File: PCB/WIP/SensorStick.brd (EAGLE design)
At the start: 74.9 x 39.4 mm, 84 parts, among them U1 TPD4F003DQDR, U10 LIS3MDLTR, U11 LIS3MDLTR, U2 BMI088, U3 BMI088, U4 BMI088, U5 STM32H743ZIT6, U9 LIS3MDLTR, Y1 ECS-TXO-3225MV-400-TR

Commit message: starting on board
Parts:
- removed AIRSPEED: 4525DO-DS5AI001DP, 4525DO-DS5AI001DP:4525DO-DS...P
- removed C3: 0.1uF, SparkFun-Capacitors:0402
- added R19, R20, R21, R22: RT0402FRE07220RL, ce-capstone:RESC1005X35N
- R6, R7: value 4.7k -> RT0402FRE07220RL; device SparkFun-Resistors:0603 -> ce-capstone:RESC1005X35N
- moved U10 561.4 mm to (62.0, 37.3)
- moved C36 544.9 mm to (14.7, 36.3)
- moved C35 536.1 mm to (9.14, 36.3)
- moved C34 502.8 mm to (11.7, 10.4)
- moved R10 501.0 mm to (53.8, 17.8)
- moved FL3 500.4 mm to (54.1, 20.1)
- moved U3 493.0 mm to (21.6, 30.7)
- moved C31 492.7 mm to (59.2, 24.4)
- moved U9 490.1 mm to (48.8, 8.13)
- moved C30 489.7 mm to (59.2, 29.5)
- moved FL1 486.2 mm to (70.9, 17.8)
- moved C29 480.3 mm to (59.2, 18.5)
- moved U11 474.0 mm to (8.13, -6.35)
- moved C32 470.2 mm to (51.1, -6.60)
- moved C33 467.9 mm to (43.7, -6.10)
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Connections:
- new net N$13: R6.2, U5.123
- new net N$14: R7.2, U5.122
- net 3V3: no longer R6.2, R7.1
- net 5V: no longer AIRSPEED.2, C3.2
- net CSB_ACCEL1: now also R19.2
- net CSB_ACCEL2: now also R21.2
- net CSB_ACCEL3: now also R6.1
- net CSB_GYRO1: now also R20.2
- net CSB_GYRO2: now also R7.1
- net CSB_GYRO3: now also U5.79
- net EXTI3: no longer AIRSPEED.5
- net GND: now also Y1.2; no longer AIRSPEED.1, C3.1
- net I2C3_SCL: no longer AIRSPEED.4, R6.1
- net I2C3_SDA: no longer AIRSPEED.3, R7.2
- net SPI1_MISO: no longer U4.10
- net SPI2_MISO: no longer U3.10
- net SPI3_MISO: no longer U2.10
- net USART2_RX: now also U5.37
- net USART2_TX: now also U5.36
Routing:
- net GND: track 69.6 -> 253.4 mm, vias 20 -> 29
- net 3V3: track 47.4 -> 206.3 mm, vias 11 -> 21
- net I2C1_SCL: track 0.00 -> 135.8 mm, vias 0 -> 7
- net I2C1_SDA: track 0.00 -> 120.3 mm, vias 0 -> 7
- net EXTI0: track 0.00 -> 101.9 mm, vias 0 -> 7
- net SPI2_MISO: track 0.00 -> 97.8 mm, vias 0 -> 6
- net EXTI2: track 0.00 -> 93.2 mm, vias 0 -> 6
- net 3V5: track 0.00 -> 87.1 mm, vias 0 -> 3
- net SPI2_SCK: track 0.00 -> 82.4 mm, vias 0 -> 2
- net SPI2_MOSI: track 0.00 -> 81.7 mm, vias 0 -> 6
- net CSB_ACCEL2: track 0.00 -> 80.7 mm, vias 0 -> 4
- net I2C3_SDA: track 23.0 -> 97.6 mm, vias 2 -> 4
- net I2C2_SCL: track 0.00 -> 73.3 mm, vias 0 -> 6
- net 3V2: track 0.00 -> 70.7 mm, vias 0 -> 4
- net IMU_INT4: track 0.00 -> 69.3 mm, vias 0 -> 8
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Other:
- board size 74.9 x 39.4 mm -> 79.5 x 48.3 mm
- board text removed: "AIR"
- board text removed: "IMU"
- board text removed: "Jesus Oviedo Noah Lutz Teagan Connon Marko Ristic Danny Cardenas"
- board text removed: "Project Dragonfly UCSB CE Capstone"

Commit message: snapshot
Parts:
- removed R22: RT0402FRE07220RL, ce-capstone:RESC1005X35N
- moved R21 112.5 mm to (72.4, 45.7)
- moved R20 110.7 mm to (54.6, 59.7), turned to 90 degrees
- moved R7 103.9 mm to (74.9, 45.7)
- moved R19 97.9 mm to (47.0, 52.1)
- moved R11 96.5 mm to (33.0, 69.8)
- moved Y1 86.0 mm to (26.7, 68.6)
- moved R9 80.1 mm to (22.9, 47.0)
- moved R8 73.4 mm to (22.9, 43.2)
- moved S2 72.0 mm to (68.6, 67.3)
- moved R3 71.4 mm to (74.9, 20.3), turned to 90 degrees
- moved D1 70.7 mm to (74.9, 25.4), turned to 90 degrees
- moved U$1 70.0 mm to (57.1, 69.8), turned to 0 degrees
- moved JST_CONNECTION 67.3 mm to (39.4, 68.6), turned to 0 degrees
- moved R6 66.1 mm to (68.6, 62.2)
- moved U11 63.7 mm to (26.7, 54.6)
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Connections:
- net SPI1_CS renamed JTDI
- new net JTRST: U5.134
- new net TRACESWO: U5.133
- net NRST: now also U5.25
- net SPI3_MISO: now also U5.112; no longer U5.134
- net SPI3_SCK: now also U5.111; no longer U5.133
- net SWCLK: now also U5.109
- net SWDIO: now also U5.105
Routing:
- net GND: track 253.4 -> 0.00 mm, vias 29 -> 0
- net 3V3: track 206.3 -> 0.00 mm, vias 21 -> 0
- net I2C1_SCL: track 135.8 -> 0.00 mm, vias 7 -> 0
- net I2C1_SDA: track 120.3 -> 0.00 mm, vias 7 -> 0
- net EXTI0: track 101.9 -> 0.00 mm, vias 7 -> 0
- net SPI2_MISO: track 97.8 -> 0.00 mm, vias 6 -> 0
- net I2C3_SDA: track 97.6 -> 0.00 mm, vias 4 -> 0
- net EXTI2: track 93.2 -> 0.00 mm, vias 6 -> 0
- net 3V5: track 87.1 -> 0.00 mm, vias 3 -> 0
- net GPIO_EXTI1: track 86.8 -> 0.00 mm, vias 3 -> 0
- net I2C3_SCL: track 83.5 -> 0.00 mm, vias 4 -> 0
- net SPI2_SCK: track 82.4 -> 0.00 mm, vias 2 -> 0
- net SPI2_MOSI: track 81.7 -> 0.00 mm, vias 6 -> 0
- net 5V: track 81.2 -> 0.00 mm
- net CSB_ACCEL2: track 80.7 -> 0.00 mm, vias 4 -> 0
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- removed copper zone on layer 15, net 3V3
- removed copper zone on layer 2, net GND
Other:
- board size 79.5 x 48.3 mm -> 77.5 x 74.6 mm
- board text removed: "**. ., ,,. ,. , *. .,. .. ,, ,. , ., ............ , ,, ., *., ** ,, .. , . ., ,, .. ., ,. ,,, *, , ./ ., ., , * .,. * ,, ,, *. .......... ...,. (*,. , ./, */. .*/ * ** .,*//,. .*/*, .* ,,. . . .* . */*/*. , ,. . , . ,. *,,*. .,,. .,, ,. .. , . ,*/,. .* .. ...,,,.. ..,. * .,. , . ,.,*. . .,./ , ..,, ,. ,,. ..,* ,*.. .,. .. ,., . , ...,,,,.. ...,,,.,,,,.... ....,.... ,, .. , * ,.,, .. ,, .. . * , *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"
- board text removed: "1"
- board text removed: "BAR"
- board text removed: "BOOT0"
- board text removed: "GPS"
- board text removed: "JST"
- board text removed: "MAG"
- board text removed: "NRST"
- board text removed: "PWR"
- board text removed: "RST"
- board text removed: "SWCLK"
- board text removed: "SWDIO"
- board text removed: "SWO"
- board text removed: "TX"

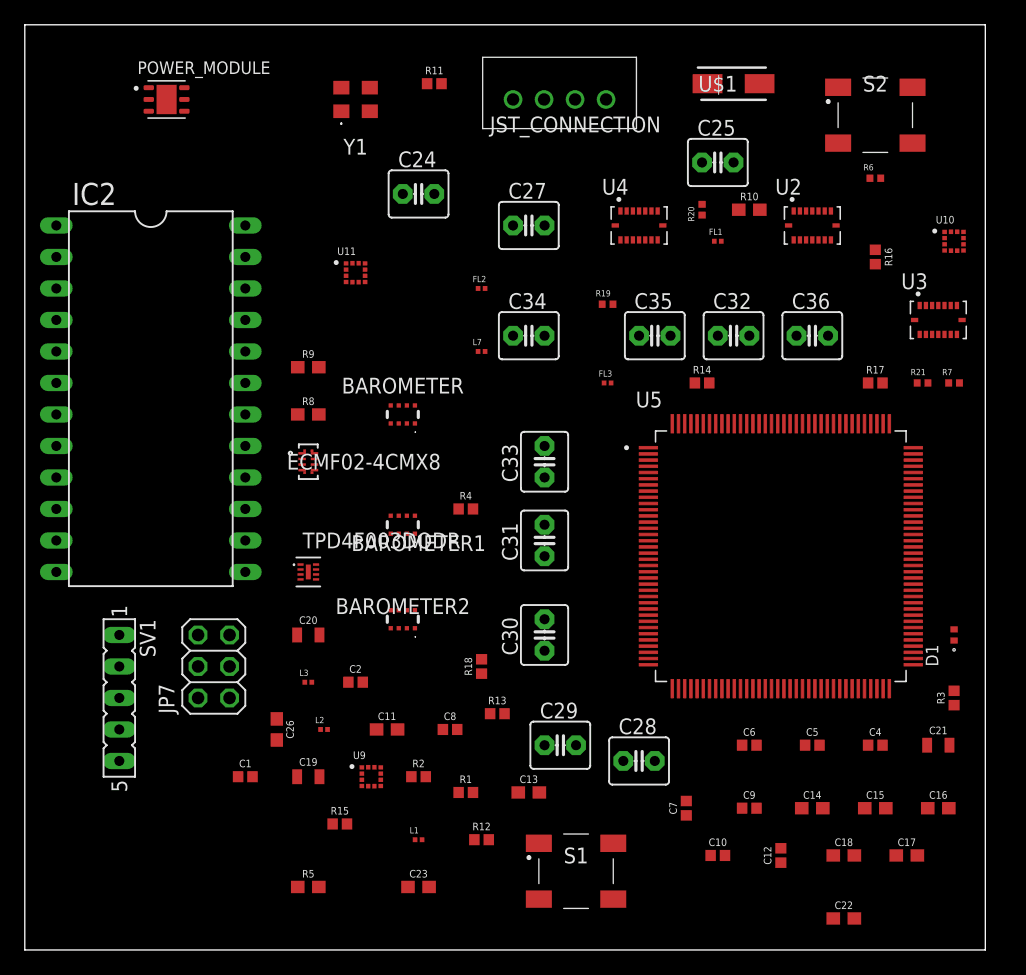
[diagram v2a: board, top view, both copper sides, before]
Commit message: added in JST connections, still need to resolve extra SPI connection
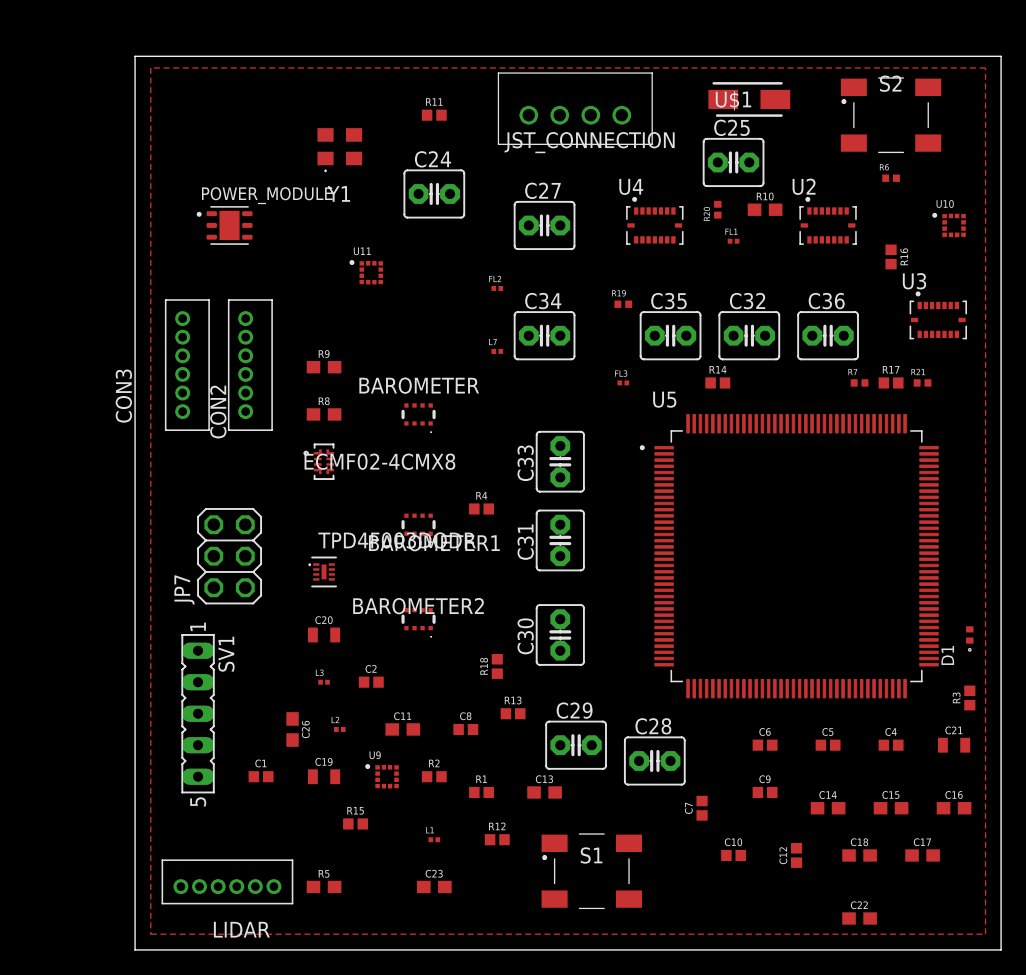
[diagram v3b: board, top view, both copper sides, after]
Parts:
- removed IC2: (no value), ic-package:DIL24-6
- added CON2, CON3, LIDAR: B6B-ZR, jst:B6B-ZR
- moved POWER_MODULE 11.4 mm to (16.5, 58.4)
- moved JP7 8.98 mm to (16.5, 31.8)
- moved R7 7.62 mm to (67.3, 45.7)
- moved SV1 6.48 mm to (14.0, 19.1)
- moved Y1 4.02 mm to (25.4, 64.8)
- moved R11 2.54 mm to (33.0, 67.3)
- moved JST_CONNECTION 1.80 mm to (40.6, 67.3)
- moved U$1 1.80 mm to (58.4, 68.6)
- moved C9 1.80 mm to (59.7, 12.7)
- moved C16 1.27 mm to (74.9, 11.4)
- moved C21 1.27 mm to (74.9, 16.5)
- moved C23 1.27 mm to (33.0, 5.08)
- moved C24 1.27 mm to (33.0, 61.0)
- moved C29 1.27 mm to (44.5, 16.5)
- moved C30 1.27 mm to (43.2, 25.4)
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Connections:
- new net N$21: LIDAR.5
- new net N$22: LIDAR.4
- net 3V3: now also LIDAR.1; no longer IC2.1, IC2.2
- net EXTI4: no longer IC2.15
- net GND: now also LIDAR.6; no longer IC2.13
- net I2C1_SCL: no longer IC2.20
- net I2C1_SDA: no longer IC2.21
- net I2C4_SCL: now also LIDAR.2
- net I2C4_SDA: now also LIDAR.3, U5.82
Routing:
- added copper zone on layer 1, net 3V3
- added copper zone on layer 2, net GND
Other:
- board size 77.5 x 74.6 mm -> 69.8 x 72.1 mm

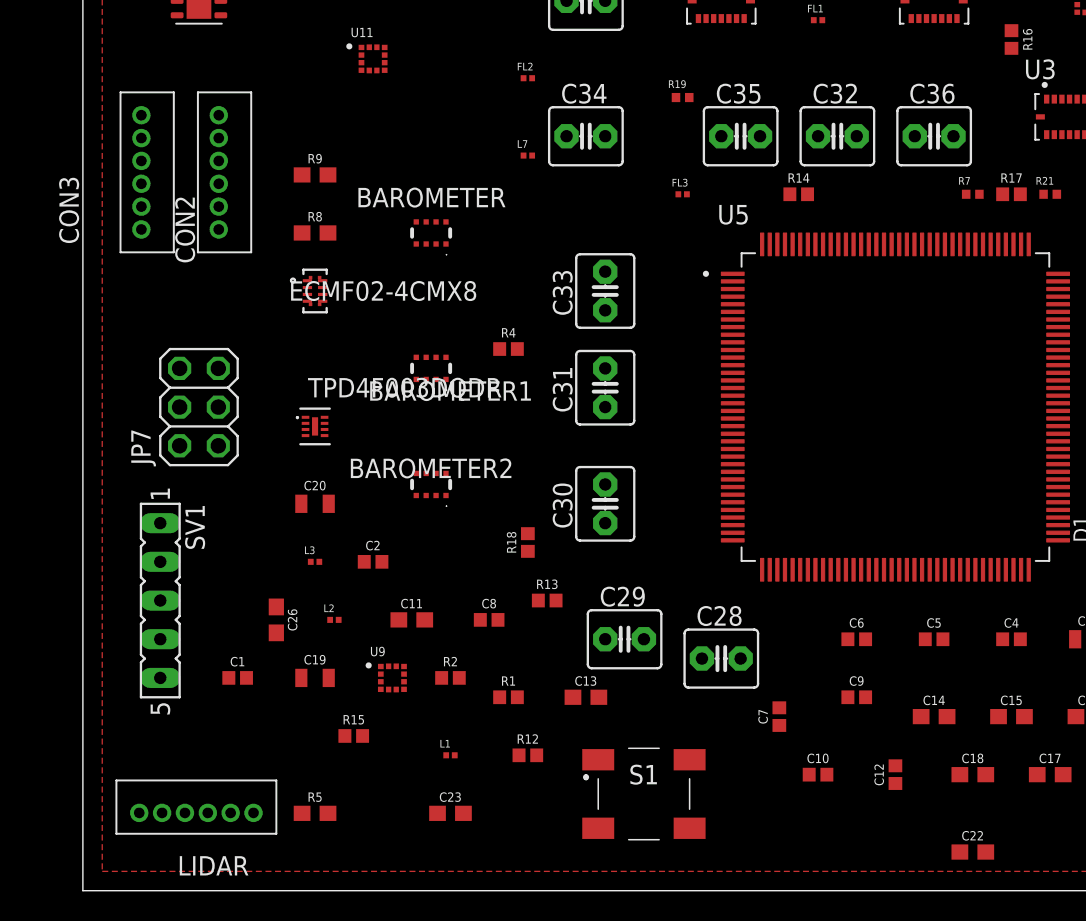
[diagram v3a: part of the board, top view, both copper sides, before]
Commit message: all jsts added, board mostly laid out, working on connections now
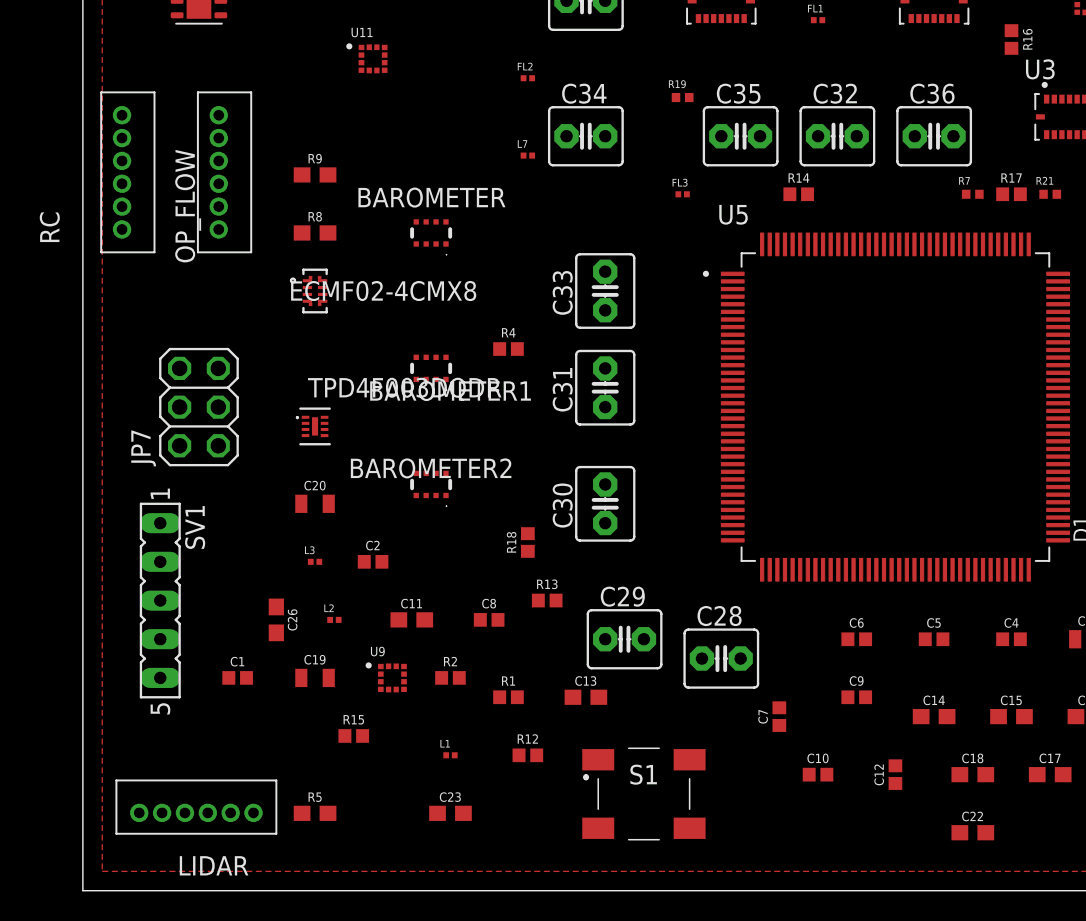
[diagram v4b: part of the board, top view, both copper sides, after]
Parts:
- removed CON3: B6B-ZR, jst:B6B-ZR
- added RC: B6B-ZR, jst:B6B-ZR
- moved C22 1.27 mm to (67.3, 3.81)
- renumbered CON2 to OP_FLOW
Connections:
- new net N$18: RC.4
- new net N$19: RC.5
- net 3V3: now also OP_FLOW.1, RC.1
- net GND: now also OP_FLOW.6, RC.6
- net SPI6_CS: now also OP_FLOW.5
- net SPI6_MISO: now also OP_FLOW.3
- net SPI6_MOSI: now also OP_FLOW.4
- net SPI6_SCK: now also OP_FLOW.2
- net UART5_RX: now also RC.3
- net UART5_TX: now also RC.2

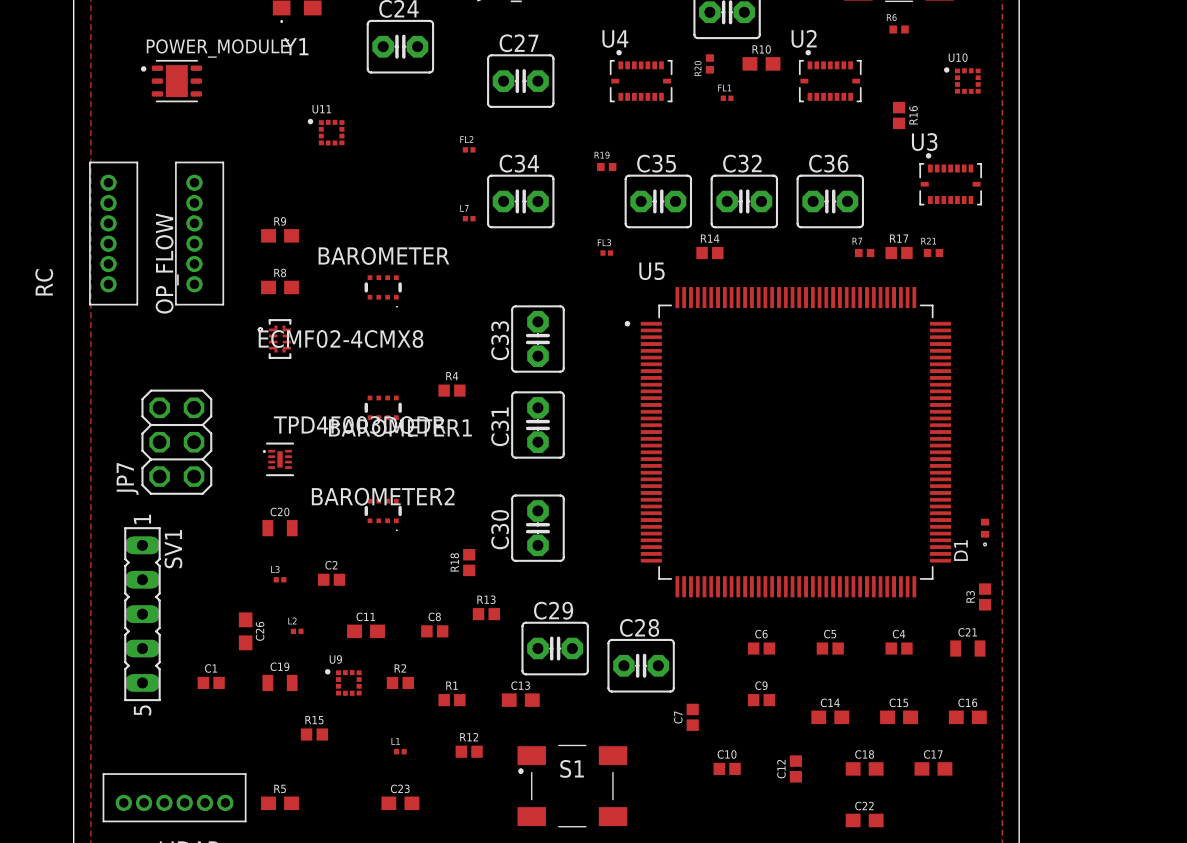
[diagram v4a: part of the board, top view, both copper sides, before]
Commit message: some minor changes with VDD, VBAT connections
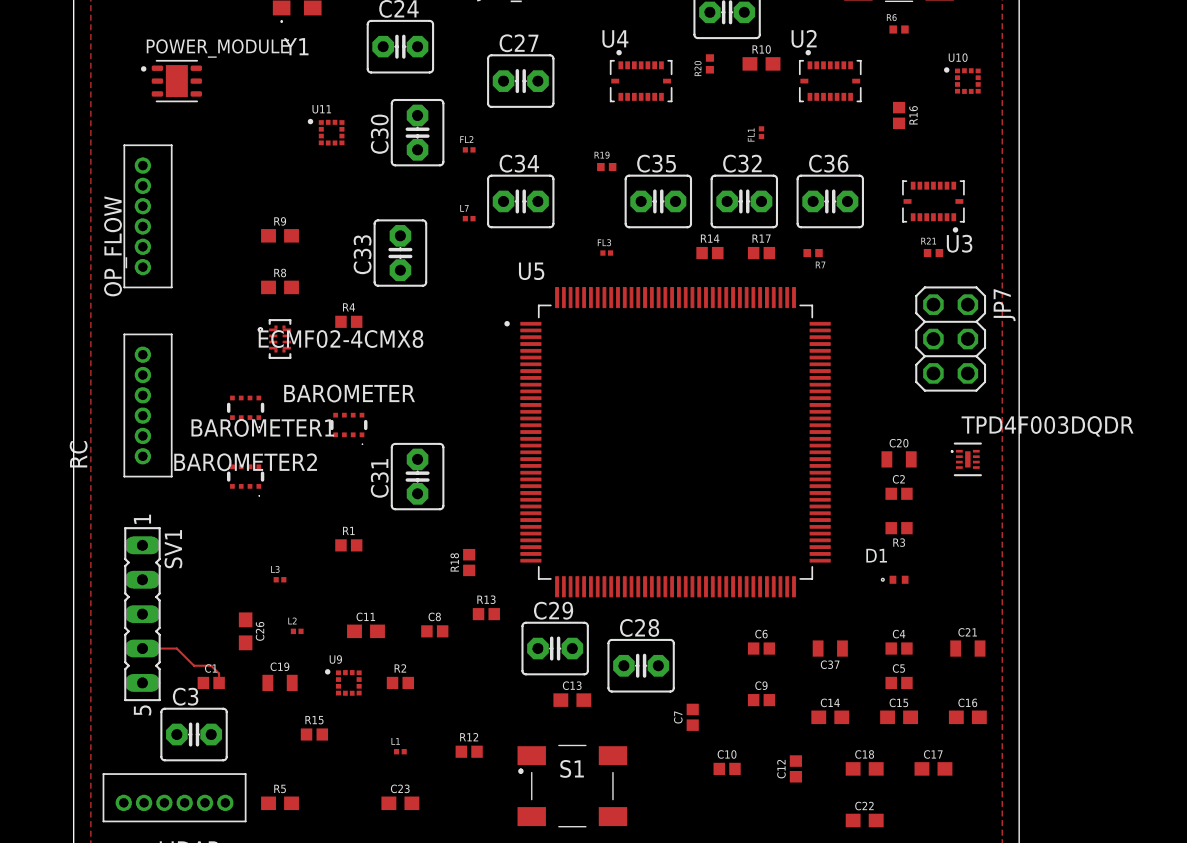
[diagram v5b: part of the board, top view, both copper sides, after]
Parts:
- added C3: 0.1uF, capacitor-wima:C2.5-4
- added C37: 1.0uF, SparkFun-Capacitors:0805
- moved JP7 57.7 mm to (73.7, 39.4), turned to 270 degrees
- moved U1 50.8 mm to (74.9, 30.5)
- moved C20 46.0 mm to (69.8, 30.5)
- moved C2 42.4 mm to (69.8, 27.9)
- moved C30 30.5 mm to (34.3, 54.6)
- moved R1 13.7 mm to (29.2, 24.1)
- moved RC 13.0 mm to (12.7, 29.2)
- moved C33 12.0 mm to (33.0, 45.7)
- moved BAROMETER2 10.5 mm to (21.6, 29.2)
- moved BAROMETER 10.5 mm to (29.2, 33.0)
- moved BAROMETER1 10.2 mm to (21.6, 34.3)
- moved R17 10.2 mm to (59.7, 45.7)
- moved C31 9.67 mm to (34.3, 29.2)
- moved R4 9.16 mm to (29.2, 40.6)
- moved U5 8.89 mm to (53.3, 31.8)
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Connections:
- removed net NRST1: U1.4
- removed net VBAT: U5.6
- removed net VCAP: U5.106, U5.71
- removed net VDD33USB: U5.95
- removed net VDDA: U5.33
- removed net VREF+: U5.32
- new net N$12: C37.1, U5.106, U5.71
- new net PDR_ON: U5.143
- net 3V3: now also C3.1, U5.33, U5.6, U5.95
- net GND: now also C3.2, C37.2
- net NRST: now also U1.4
- net VREF: now also U5.32
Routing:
- net GND: track 0.00 -> 7.12 mm
- net 3V3: track 0.00 -> 1.27 mm

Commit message: fixing connections XD
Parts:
- added R22, R25: 0, SparkFun-Resistors:0603
- added R23, R24: 22, SparkFun-Resistors:0402
- C24, C25, C27, C28, C29, C30, C31, C32, C33: value (none) -> 0.1uf
- moved U2 1.27 mm to (64.8, 57.1)
- moved R16 1.27 mm to (69.8, 57.1)
- moved U4 1.27 mm to (50.8, 59.7)
- moved U5 1.27 mm to (54.6, 31.8)
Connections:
- removed net PDR_ON: U5.143
- removed net TRACESWO: U5.133
- removed net VSSA: U5.31
- new net EXTI0_1: R23.2, U2.16
- new net EXTI1: U3.16
- new net EXTI1_1: R24.2, U2.12
- new net GPIO_EXTI0_1: R23.1, U5.56
- new net GPIO_EXTI1_1: R24.1, U5.57
- new net IMU_INT1: R22.1, U3.1
- new net IMU_INT3: R22.2, U3.13
- new net IMU_INT5: R25.1, U2.1
- new net IMU_INT6: R25.2, U2.13
- new net N$15: R19.1, U5.58
- new net N$16: R20.1, U5.59
- new net N$17: R21.1, U5.60
- net 3V3: now also L1.2, U5.143, U5.31; no longer L1.1
- net EXTI0: no longer U2.16, U3.16
- net EXTI2: no longer U2.12, U3.12
- net EXTI3: now also U3.12
- net IMU_INT2: no longer U2.1, U3.1
- net IMU_INT4: no longer U2.13, U3.13
- net SWO: now also U5.133
- net VREF: now also L1.1; no longer L1.2
